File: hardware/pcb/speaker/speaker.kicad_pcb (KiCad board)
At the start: 4 copper layers, 55.4 x 64 mm, 55 parts, among them J1 JST SH BM02B Connector, J2 JST SH BM02B Connector, J3 JST SH BM02B Connector, J4 JST SH BM02B Connector, J5 JST SH BM02B Connector, J6 JST SH BM02B Connector, J7 Conn_01x02, M1 Ultrasonic_Transducer, M10 Ultrasonic_Transducer, M11 Ultrasonic_Transducer, M12 Ultrasonic_Transducer, M13 Ultrasonic_Transducer, M14 Ultrasonic_Transducer, M15 Ultrasonic_Transducer, M16 Ultrasonic_Transducer, M17 Ultrasonic_Transducer, M18 Ultrasonic_Transducer, M19 Ultrasonic_Transducer, M2 Ultrasonic_Transducer, M3 Ultrasonic_Transducer, M4 Ultrasonic_Transducer, M5 Ultrasonic_Transducer, M6 Ultrasonic_Transducer, M7 Ultrasonic_Transducer, M8 Ultrasonic_Transducer, M9 Ultrasonic_Transducer, U1 LTC2631-Z, U2 LM2735XMF

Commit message: REWORK pcb design
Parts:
- removed JP1: Jumper_2_Open, Jumper:SolderJumper-2_P1.3mm_Bridged2Bar_Pad1.0x1.5mm
- removed REF** (x4): MountingHole_2.2mm_M2, MountingHole:MountingHole_2.2mm_M2
- added C10: 100nF, Capacitor_SMD:C_0805_2012Metric, B.Cu at (139.0, 76.8)
- added C11: 100nF, Capacitor_SMD:C_0805_2012Metric, B.Cu at (150.7, 66.3)
- added C8: 100nF, Capacitor_SMD:C_0805_2012Metric, B.Cu at (137.3, 87.9)
- added C9: 82nF, Capacitor_SMD:C_0805_2012Metric, B.Cu at (127.0, 83.3)
- added R8: 15k, Resistor_SMD:R_0805_2012Metric, B.Cu at (136.4, 85.0)
- added R9: 15k, Resistor_SMD:R_0805_2012Metric, B.Cu at (138.3, 82.9)
- C7: value 330pF -> 470pF
- L1: value 15uF -> 10uF; footprint Inductor_SMD:L_1206_3216Metric -> Inductor_SMD:L_Wuerth_5030_Handsolder
- R4: value 5k -> 10k
- R5, R6: value 1.7k -> 1.5k
- moved C1 22.7 mm to (146.7, 72.7), turned to -90 degrees
- moved TP1 20.4 mm to (136.9, 53.8)
- moved C2 19.0 mm to (130.8, 55.1)
- moved TP2 16.9 mm to (126.0, 73.4)
- moved R7 15.2 mm to (147.2, 58.4)
- moved R2 11.5 mm to (143.1, 57.9), turned to 0 degrees
- moved L1 11.5 mm to (144.7, 66.4), turned to 0 degrees
- moved C7 11.3 mm to (143.1, 53.5), turned to 180 degrees
- moved R1 11.0 mm to (143.1, 55.7), turned to 180 degrees
- moved U2 10.2 mm to (143.6, 60.8), turned to 0 degrees
- moved D1 10.1 mm to (135.3, 61.5), turned to -90 degrees
- moved TP3 9.89 mm to (143.5, 87.8)
- moved C6 7.08 mm to (130.7, 77.5), turned to 180 degrees
- moved OP1 5.54 mm to (135.9, 79.9)
- moved R3 5.45 mm to (133.8, 82.9)
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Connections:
- C2 pad 1: Net-(C2-Pad1) -> +24V
- C7 pad 1: Net-(C2-Pad1) -> +24V
- D1 pad 1: Net-(C2-Pad1) -> +24V
- L1 pad 1: +5V -> Net-(D1-Pad2)
- L1 pad 2: Net-(D1-Pad2) -> +5V
- OP1 pad 1: /Trancducer Sig -> Net-(OP1-Pad1)
- OP1 pad 3: /Audio Sig -> Net-(C8-Pad2)
- R1 pad 1: Net-(C2-Pad1) -> +24V
- R3 pad 1: /Trancducer Sig -> Net-(OP1-Pad1)
- R4 pad 2: GND -> Net-(C9-Pad2)
- TP1 pad 1: Net-(C2-Pad1) -> +24V
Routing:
- net Net-(C2-Pad1): track 20.9 -> 0.00 mm
- net +5V: track 14.2 -> 0.00 mm, vias 7 -> 0
- net Net-(D1-Pad2): track 11.8 -> 0.00 mm
- net /Trancducer Sig: track 193.2 -> 182.3 mm
- net /Audio Sig: track 15.7 -> 9.04 mm
- net Net-(C8-Pad2): track 0.00 -> 6.17 mm
- net Net-(OP1-Pad1): track 0.00 -> 5.49 mm
- net /SDA: track 136.7 -> 133.3 mm, vias 6 -> 7
- net Net-(JP2-Pad2): track 16.9 -> 13.9 mm, vias 0 -> 2
- net +24V: track 7.36 -> 4.59 mm, vias 0 -> 20
- net GND: track 43.0 -> 40.8 mm, vias 7 -> 8
- net /SCL: track 136.5 -> 134.4 mm, vias 4 -> 10
- net Net-(C9-Pad2): track 0.00 -> 1.94 mm
- net Net-(OP1-Pad4): track 3.88 -> 5.72 mm
- net Net-(JP3-Pad2): track 6.66 -> 5.36 mm
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- added copper zone on B.Cu, net +24V
- added copper zone on F.Cu, net +24V
- added copper zone on In2.Cu, net GND
- added copper zone on B.Cu, net Net-(D1-Pad2)
- added copper zone on B.Cu, net Net-(OP1-Pad1)
- removed copper zone on In2.Cu, net +5V
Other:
- rule pad_to_mask_clearance: 0 -> 0.2
- rule solder_mask_min_width: 0.1016 -> 0.05

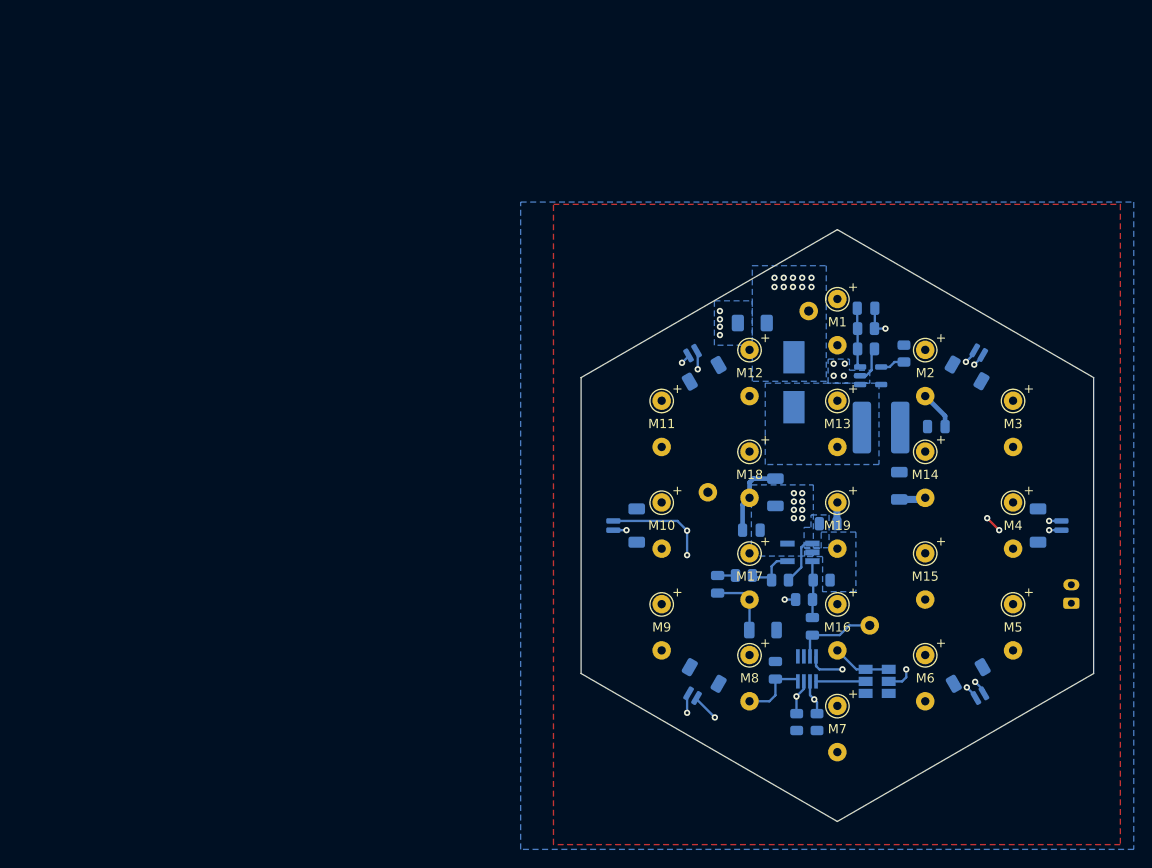
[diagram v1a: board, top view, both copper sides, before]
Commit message: REWORK pcb layout, ADD BOM
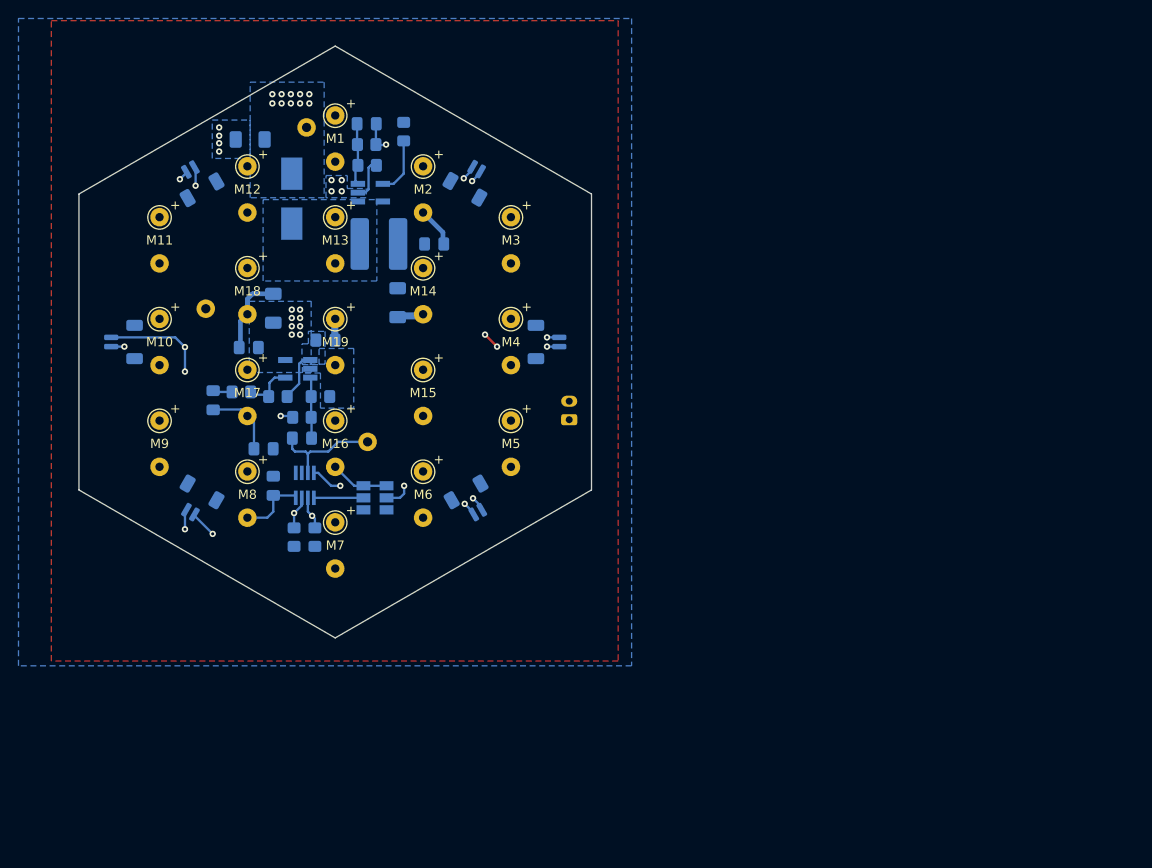
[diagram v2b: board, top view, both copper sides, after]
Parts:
- C1, C5: footprint Capacitor_SMD:C_1206_3216Metric -> Capacitor_SMD:C_1206_3216Metric_Pad1.33x1.80mm_HandSolder
- C10, C11, C4, C6, C7, C8, C9: footprint Capacitor_SMD:C_0805_2012Metric -> Capacitor_SMD:C_0805_2012Metric_Pad1.18x1.45mm_HandSolder
- C3: footprint Capacitor_SMD:C_1206_3216Metric -> Capacitor_SMD:C_0805_2012Metric_Pad1.18x1.45mm_HandSolder
- L1: value 10uF -> 10uH
- R1, R2, R3, R4, R5, R6, R7, R8, R9: footprint Resistor_SMD:R_0805_2012Metric -> Resistor_SMD:R_0805_2012Metric_Pad1.20x1.40mm_HandSolder
- U2: footprint Package_TO_SOT_SMD:SOT-23-5 -> Package_TO_SOT_SMD:SOT-23-5_HandSoldering
- moved R7 59.2 mm to (93.1, 34.4)
- moved C8 58.8 mm to (82.1, 67.5), turned to 0 degrees
- moved C9 58.1 mm to (72.5, 63.5)
- moved R6 57.9 mm to (81.2, 78.2)
- moved R5 57.9 mm to (83.5, 78.2)
- moved R4 57.9 mm to (75.5, 62.5)
- moved C10 57.9 mm to (84.7, 57.0)
- moved C4 57.8 mm to (79.0, 72.7)
- moved C5 57.8 mm to (79.0, 53.5)
- moved C6 57.8 mm to (76.3, 57.8)
- moved C2 57.8 mm to (76.5, 35.2)
- moved D1 57.8 mm to (81.0, 41.6)
- moved J4 57.8 mm to (108.6, 57.1)
- moved J7 57.8 mm to (111.0, 65.5)
- moved JP2 57.8 mm to (91.2, 74.0)
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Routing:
- net Net-(R7-Pad2): track 2.69 -> 6.26 mm
- net /Audio Sig: track 9.04 -> 12.1 mm
- net GND: track 40.8 -> 41.6 mm
- net Net-(JP2-Pad2): track 13.9 -> 13.3 mm
- net Net-(C8-Pad2): track 6.17 -> 6.71 mm

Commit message: REV 3
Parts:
- added C12: 1nF, Capacitor_SMD:C_0805_2012Metric_Pad1.18x1.45mm_HandSolder, B.Cu at (75.8, 57.5)
- added C13: 1nF, Capacitor_SMD:C_0805_2012Metric_Pad1.18x1.45mm_HandSolder, B.Cu at (76.3, 32.6)
- moved C6 7.43 mm to (82.0, 52.9), turned to 90 degrees
- moved R6 4.86 mm to (79.3, 82.7)
- moved C7 4.07 mm to (87.1, 30.0), turned to 0 degrees
- moved R5 4.05 mm to (81.5, 81.8)
- moved TP2 3.11 mm to (74.0, 51.4)
- moved R1 2.09 mm to (87.2, 35.0), turned to 0 degrees
- moved C5 1.10 mm to (79.0, 52.4)
- moved D1 0.91 mm to (81.9, 41.5)
- moved C11 0.54 mm to (96.8, 46.2)
- moved C1 0.30 mm to (92.2, 53.0)
- moved C2 0.30 mm to (76.5, 35.5)
- moved TP1 0.20 mm to (82.8, 34.0)
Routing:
- net GND: track 41.6 -> 9.62 mm, vias 8 -> 18
- net +5V: track 0.00 -> 12.1 mm, vias 0 -> 17
- net /SDA: track 133.0 -> 137.9 mm, vias 7 -> 9
- net Net-(C7-Pad2): track 6.60 -> 10.1 mm
- net +24V: track 4.89 -> 1.39 mm, vias 20 -> 19
- net /SCL: track 134.2 -> 136.0 mm, vias 10 -> 7
- added copper zone on In1.Cu, net +24V
- added copper zone on In1.Cu, net +5V
- added copper zone on F.Cu, net GND
- removed copper zone on F.Cu, net +24V
- removed copper zone on In1.Cu, net GND

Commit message: add pcb gbr files
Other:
- rule pad_to_mask_clearance: 0.2 -> 0

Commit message: update gerber files
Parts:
- R1: value 91k -> 180k
- moved C10 0.05 mm to (84.6, 57.0)

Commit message: REWORK PCB design
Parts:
- removed JP2, JP3: Jumper_3_Open, Jumper:SolderJumper-3_P1.3mm_Open_Pad1.0x1.5mm_NumberLabels
- removed R5, R6: 1.5k, Resistor_SMD:R_0805_2012Metric_Pad1.20x1.40mm_HandSolder
- added C14: 10uF, Capacitor_SMD:C_1206_3216Metric_Pad1.33x1.80mm_HandSolder, B.Cu at (75.8, 51.9)
- added C15: 100nF, Capacitor_SMD:C_0805_2012Metric_Pad1.18x1.45mm_HandSolder, B.Cu at (84.4, 52.0)
- added H1: MountingHole_Pad, MountingHole:MountingHole_2.2mm_M2_DIN965_Pad_TopBottom, B.Cu at (60.8, 42.8)
- added H2: MountingHole_Pad, MountingHole:MountingHole_2.2mm_M2_DIN965_Pad_TopBottom, B.Cu at (60.8, 71.5)
- added H3: MountingHole_Pad, MountingHole:MountingHole_2.2mm_M2_DIN965_Pad_TopBottom, B.Cu at (110.6, 71.5)
- added H4: MountingHole_Pad, MountingHole:MountingHole_2.2mm_M2_DIN965_Pad_TopBottom, B.Cu at (110.6, 42.8)
- added Q1: BC847, Package_TO_SOT_SMD:SOT-23, B.Cu at (80.5, 54.2)
- added Q2: BC857, Package_TO_SOT_SMD:SOT-23, B.Cu at (80.5, 58.7)
- added R10: 100k, Resistor_SMD:R_0805_2012Metric_Pad1.20x1.40mm_HandSolder, B.Cu at (90.7, 58.3)
- added R11: 100k, Resistor_SMD:R_0805_2012Metric_Pad1.20x1.40mm_HandSolder, B.Cu at (94.5, 68.0)
- C10: value 100nF -> 1uF; footprint Capacitor_SMD:C_0805_2012Metric_Pad1.18x1.45mm_HandSolder -> Capacitor_SMD:C_1206_3216Metric_Pad1.33x1.80mm_HandSolder
- C8: value 100nF -> 1.5nF
- C9: value 82nF -> 10nF
- J1, J2, J3, J4, J5, J6: value JST SH BM02B Connector -> Conn_01x03; footprint Connector_JST:JST_SH_BM02B-SRSS-TB_1x02-1MP_P1.00mm_Vertical -> custom_footprints:SPI_Conn_SMD
- J7: footprint Connector_JST:JST_PH_B2B-PH-K_1x02_P2.00mm_Vertical -> Connector_PinHeader_2.54mm:PinHeader_1x02_P2.54mm_Vertical_SMD_Pin1Left
- R3: value 10k -> 15k
- R4: value 10k -> 5k
- R8, R9: value 15k -> 100k
- U1: value LTC2631-Z -> LTC2640-Z; footprint custom_footprints:LTC2631-Z -> Package_TO_SOT_SMD:SOT-23-8_Handsoldering
- moved J6 36.1 mm to (101.2, 38.3), turned to -120 degrees
- moved J1 36.1 mm to (70.2, 38.4), turned to -60 degrees
- moved J4 20.3 mm to (101.2, 76.0), turned to 120 degrees
- moved J3 20.2 mm to (70.1, 76.0), turned to 60 degrees
- moved J5 20.0 mm to (109.8, 57.2), turned to 180 degrees
- moved J2 19.8 mm to (61.6, 57.2), turned to 0 degrees
- moved J7 14.2 mm to (99.5, 57.3)
- moved C5 14.0 mm to (72.5, 64.7), turned to 0 degrees
- moved C6 13.6 mm to (71.2, 61.2)
- moved C4 9.04 mm to (88.0, 74.0)
- moved U1 8.66 mm to (91.2, 74.3)
- moved C3 7.02 mm to (83.5, 73.0)
- moved R4 6.12 mm to (77.7, 68.3)
- moved R9 5.95 mm to (83.0, 68.9), turned to -90 degrees
- moved C9 5.89 mm to (74.2, 69.1)
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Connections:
- J1 pad 1: /SDA -> /CS
- J2 pad 1: /SDA -> /CS
- J3 pad 1: /SDA -> /CS
- J4 pad 1: /SDA -> /CS
- J5 pad 1: /SDA -> /CS
- J6 pad 1: /SDA -> /CS
- OP1 pad 1: Net-(C10-Pad1) -> Net-(OP1-Pad1)
- R3 pad 1: Net-(C10-Pad1) -> Net-(OP1-Pad4)
- R3 pad 2: Net-(OP1-Pad4) -> Net-(C10-Pad1)
- U1 pad 1: Net-(JP3-Pad2) -> /CS
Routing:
- net /CS: track 0.00 -> 135.1 mm, vias 0 -> 6
- net /SCL: track 136.0 -> 120.7 mm, vias 7 -> 2
- net Net-(C10-Pad1): track 5.49 -> 17.9 mm, vias 0 -> 2
- net +24V: track 1.39 -> 13.2 mm, vias 19 -> 9
- net GND: track 9.62 -> 0.00 mm, vias 18 -> 20
- net Net-(R11-Pad2): track 13.3 -> 5.50 mm, vias 2 -> 0
- net Net-(OP1-Pad1): track 0.00 -> 7.61 mm
- net /Trancducer Sig: track 182.3 -> 188.4 mm
- net Net-(JP3-Pad2): track 5.36 -> 0.00 mm
- net Net-(C8-Pad2): track 6.71 -> 10.7 mm
- net /Audio Sig: track 12.1 -> 8.41 mm
- net Net-(OP1-Pad4): track 5.80 -> 4.27 mm
- net +5V: track 12.1 -> 11.2 mm, vias 17 -> 10
- net Net-(C7-Pad2): track 10.1 -> 9.42 mm
- net /SDA: track 137.9 -> 138.3 mm, vias 9 -> 4
- removed copper zone on B.Cu, net Net-(C10-Pad1)

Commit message: UPDATE BOM
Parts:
- C3: footprint Capacitor_SMD:C_0805_2012Metric_Pad1.18x1.45mm_HandSolder -> Capacitor_SMD:C_1206_3216Metric_Pad1.33x1.80mm_HandSolder
- moved C3 0.50 mm to (83.0, 73.0)
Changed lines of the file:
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@@
     )
   )
-  (footprint "Capacitor_SMD:C_0805_2012Metric_Pad1.18x1.45mm_HandSolder" (layer "B.Cu")
-    (at 83.5 73 180)
-    (descr "Capacitor SMD 0805 (2012 Metric), square (rectangular) end terminal, IPC_7351 nominal with elongated pad for handsoldering. (Body size source: IPC-SM-782 page 76, https://www.pcb-3d.com/wordpress/wp-content/uploads/ipc-sm-782a_amendment_1_and_2.pdf, https://docs.google.com/spreadsheets/d/1BsfQQcO9C6DZCsRaXUlFlo91Tg2WpOkGARC1WS5S8t0/edit?usp=sharing), generated with kicad-footprint-generator")
+  (footprint "Capacitor_SMD:C_1206_3216Metric_Pad1.33x1.80mm_HandSolder" (layer "B.Cu")
+    (at 83 72.95 180)
+    (descr "Capacitor SMD 1206 (3216 Metric), square (rectangular) end terminal, IPC_7351 nominal with elongated pad for handsoldering. (Body size source: IPC-SM-782 page 76, https://www.pcb-3d.com/wordpress/wp-content/uploads/ipc-sm-782a_amendment_1_and_2.pdf), generated with kicad-footprint-generator")
     (tags "capacitor handsolder")
     (property "Sheetfile" "speaker.kicad_sch")
     (property "Sheetname" "")
     (attr smd)
-    (fp_text reference "C3" (at 0.45 -1.8) (layer "B.SilkS")
-      (effects (font (size 1 1) (thickness 0.15)) (justify mirror))
-    )
-    (fp_text value "10uF" (at 0 -1.68) (layer "B.Fab")
-      (effects (font (size 1 1) (thickness 0.15)) (justify mirror))
-    )
-    (fp_text user "${REFERENCE}" (at 0 0) (layer "B.Fab")
-      (effects (font (size 0.5 0.5) (thickness 0.08)) (justify mirror))
-    )
-    (fp_line (start -0.261252 0.735) (end 0.261252 0.735) (layer "B.SilkS") (width 0.12))
-    (fp_line (start -0.261252 -0.735) (end 0.261252 -0.735) (layer "B.SilkS") (width 0.12))
-    (fp_line (start -1.88 -0.98) (end -1.88 0.98) (layer "B.CrtYd") (width 0.05))
-    (fp_line (start -1.88 0.98) (end 1.88 0.98) (layer "B.CrtYd") (width 0.05))
-    (fp_line (start 1.88 0.98) (end 1.88 -0.98) (layer "B.CrtYd") (width 0.05))
-    (fp_line (start 1.88 -0.98) (end -1.88 -0.98) (layer "B.CrtYd") (width 0.05))
-    (fp_line (start 1 -0.625) (end -1 -0.625) (layer "B.Fab") (width 0.1))
-    (fp_line (start -1 0.625) (end 1 0.625) (layer "B.Fab") (width 0.1))
-    (fp_line (start -1 -0.625) (end -1 0.625) (layer "B.Fab") (width 0.1))
-    (fp_line (start 1 0.625) (end 1 -0.625) (layer "B.Fab") (width 0.1))
-    (pad "1" smd roundrect (at -1.0375 0 180) (size 1.175 1.45) (layers "B.Cu" "B.Paste" "B.Mask") (roundrect_rratio 0.212766)
+    (fp_text reference "C3" (at 0 -2) (layer "B.SilkS")
+      (effects (font (size 1 1) (thickness 0.15)) (justify mirror))
+    )
+    (fp_text value "10uF" (at 0 -1.85) (layer "B.Fab")
+      (effects (font (size 1 1) (thickness 0.15)) (justify mirror))
+    )
+    (fp_text user "${REFERENCE}" (at 0 0) (layer "B.Fab")
+      (effects (font (size 0.8 0.8) (thickness 0.12)) (justify mirror))
+    )
+    (fp_line (start -0.711252 -0.91) (end 0.711252 -0.91) (layer "B.SilkS") (width 0.12))
+    (fp_line (start -0.711252 0.91) (end 0.711252 0.91) (layer "B.SilkS") (width 0.12))
+    (fp_line (start 2.48 1.15) (end 2.48 -1.15) (layer "B.CrtYd") (width 0.05))
+    (fp_line (start 2.48 -1.15) (end -2.48 -1.15) (layer "B.CrtYd") (width 0.05))
+    (fp_line (start -2.48 1.15) (end 2.48 1.15) (layer "B.CrtYd") (width 0.05))
+    (fp_line (start -2.48 -1.15) (end -2.48 1.15) (layer "B.CrtYd") (width 0.05))
+    (fp_line (start 1.6 0.8) (end 1.6 -0.8) (layer "B.Fab") (width 0.1))
+    (fp_line (start 1.6 -0.8) (end -1.6 -0.8) (layer "B.Fab") (width 0.1))
+    (fp_line (start -1.6 -0.8) (end -1.6 0.8) (layer "B.Fab") (width 0.1))
+    (fp_line (start -1.6 0.8) (end 1.6 0.8) (layer "B.Fab") (width 0.1))
+    (pad "1" smd roundrect (at -1.5625 0 180) (size 1.325 1.8) (layers "B.Cu" "B.Paste" "B.Mask") (roundrect_rratio 0.188679)
       (net 1 "+5V") (pintype "passive"))
-    (pad "2" smd roundrect (at 1.0375 0 180) (size 1.175 1.45) (layers "B.Cu" "B.Paste" "B.Mask") (roundrect_rratio 0.212766)
+    (pad "2" smd roundrect (at 1.5625 0 180) (size 1.325 1.8) (layers "B.Cu" "B.Paste" "B.Mask") (roundrect_rratio 0.188679)
       (net 2 "GND") (pintype "passive"))
-    (model "${KICAD6_3DMODEL_DIR}/Capacitor_SMD.3dshapes/C_0805_2012Metric.wrl"
+    (model "${KICAD6_3DMODEL_DIR}/Capacitor_SMD.3dshapes/C_1206_3216Metric.wrl"
       (offset (xyz 0 0 0))
       (scale (xyz 1 1 1))
@@
   (via (at 85.35 41.15) (size 0.6) (drill 0.35) (layers "F.Cu" "B.Cu") (free) (net 2))
   (via (at 72.6 59) (size 0.6858) (drill 0.35) (layers "F.Cu" "B.Cu") (free) (net 2))
-  (via (at 80.85 73) (size 0.6858) (drill 0.35) (layers "F.Cu" "B.Cu") (free) (net 2))
+  (via (at 79.85 72.95) (size 0.6858) (drill 0.35) (layers "F.Cu" "B.Cu") (free) (net 2))
   (via (at 87.4 76.65) (size 0.6858) (drill 0.35) (layers "F.Cu" "B.Cu") (free) (net 2))
   (via (at 91.7 56.4) (size 0.6) (drill 0.35) (layers "F.Cu" "B.Cu") (free) (net 2))
